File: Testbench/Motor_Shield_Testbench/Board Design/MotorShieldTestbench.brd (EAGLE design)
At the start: 63.5 x 87.6 mm, 49 parts, among them IC2 74LS04D, IC3 74AC74D, IC4 74AC74D, U1 ATMEGA2560AU, U10 +12v, U2 FT232RL, U3 ATTINY85-20SU, U4 ATTINY85-20SU, U6 SN74LVC2G157DCTR, U7 SN74LVC2G157DCTR, U8 SN74LVC2G157DCTR, U9 SN74LVC2G157DCTR, X4 2510-, X5 2510-, X6 MINI-USB_4P-32005-101

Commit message: complete board v1
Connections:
- net LDIR: now also U1.83; no longer U1.76
- net RSPEED: now also U1.84; no longer U1.83
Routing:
- net D+: track 214.0 -> 39.0 mm, vias 0 -> 2
- net +5V: track 509.0 -> 500.6 mm
- net LWAVE1: track 62.6 -> 54.4 mm, vias 6 -> 5
- net GND: track 107.9 -> 102.6 mm
- net D-: track 74.1 -> 69.8 mm
- net RDIR: track 20.2 -> 23.7 mm, vias 3 -> 1
- net TXM: track 15.3 -> 17.5 mm, vias 2 -> 0
- net RXM: track 22.7 -> 21.3 mm
- net LSPEED: track 18.0 -> 19.2 mm, vias 2 -> 0

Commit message: Set layers and DRC
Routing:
- net LWAVE1: track 54.4 -> 56.2 mm

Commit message: minor improvements
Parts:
- moved X5 61.1 mm to (45.0, 11.5)
- moved X4 60.9 mm to (54.0, 11.5), turned to 90 degrees
- moved R13 44.3 mm to (49.0, 59.0)
- moved LED3 42.1 mm to (52.2, 57.5), turned to 270 degrees
- moved R8 39.6 mm to (26.0, 40.0)
- moved R7 38.7 mm to (26.0, 42.0)
- moved LED2 37.4 mm to (22.0, 40.0), turned to 180 degrees
- moved C10 35.0 mm to (10.5, 36.5)
- moved R1 34.2 mm to (39.2, 5.75), turned to 270 degrees
- moved R2 33.0 mm to (39.2, 9.50), turned to 270 degrees
- moved LED1 33.0 mm to (22.0, 42.0), turned to 180 degrees
- moved U10 27.6 mm to (11.5, 58.0), turned to 0 degrees
- moved IC4 27.5 mm to (32.5, 6.50), turned to 270 degrees
- moved IC3 26.6 mm to (32.5, 27.5), turned to 270 degrees
- moved U2 26.5 mm to (14.0, 44.5), turned to 180 degrees
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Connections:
- net LE1: now also U1.4
- net LE2: now also U1.5
- net LSELECT: now also IC2.13; no longer IC2.1
- net LWAVE: now also IC2.11; no longer IC2.9
- net N$14: now also IC2.4; no longer IC2.10
- net N$27: now also IC2.10; no longer IC2.8
- net N$3: now also IC2.2; no longer IC2.4
- net N$8: now also IC2.12; no longer IC2.2
- net RDIR: now also U1.85; no longer U1.77
- net RE1: now also U1.45
- net RE2: now also U1.46
- net RSELECT: now also IC2.1; no longer IC2.3
- net RWAVE: now also IC2.3; no longer IC2.11
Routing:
- net +5V: track 500.6 -> 134.5 mm, vias 10 -> 18
- net LWAVE2: track 116.6 -> 19.2 mm
- net RE2: track 31.3 -> 106.8 mm, vias 0 -> 4
- net D-: track 69.8 -> 5.20 mm
- net RE1: track 18.8 -> 82.7 mm, vias 0 -> 2
- net LDIR: track 11.7 -> 74.2 mm
- net RWAVE1: track 68.7 -> 9.14 mm, vias 2 -> 0
- net LE1: track 21.6 -> 76.5 mm, vias 0 -> 4
- net RDIR: track 23.7 -> 77.8 mm, vias 1 -> 0
- net RSPEEDH: track 6.08 -> 60.2 mm
- net LSPEEDH: track 7.15 -> 55.2 mm
- net GND: track 102.6 -> 55.0 mm, vias 30 -> 42
- net LWAVE1: track 56.2 -> 8.98 mm, vias 5 -> 0
- net RWAVE2: track 63.5 -> 20.3 mm, vias 5 -> 0
- net RSPEED: track 47.0 -> 12.1 mm
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- added copper zone on layer 1, net +5V
- added copper zone on layer 1, net GND
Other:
- board size 63.5 x 87.6 mm -> 60 x 67 mm
- board text added: "MotorShieldTestbench Example Routing"

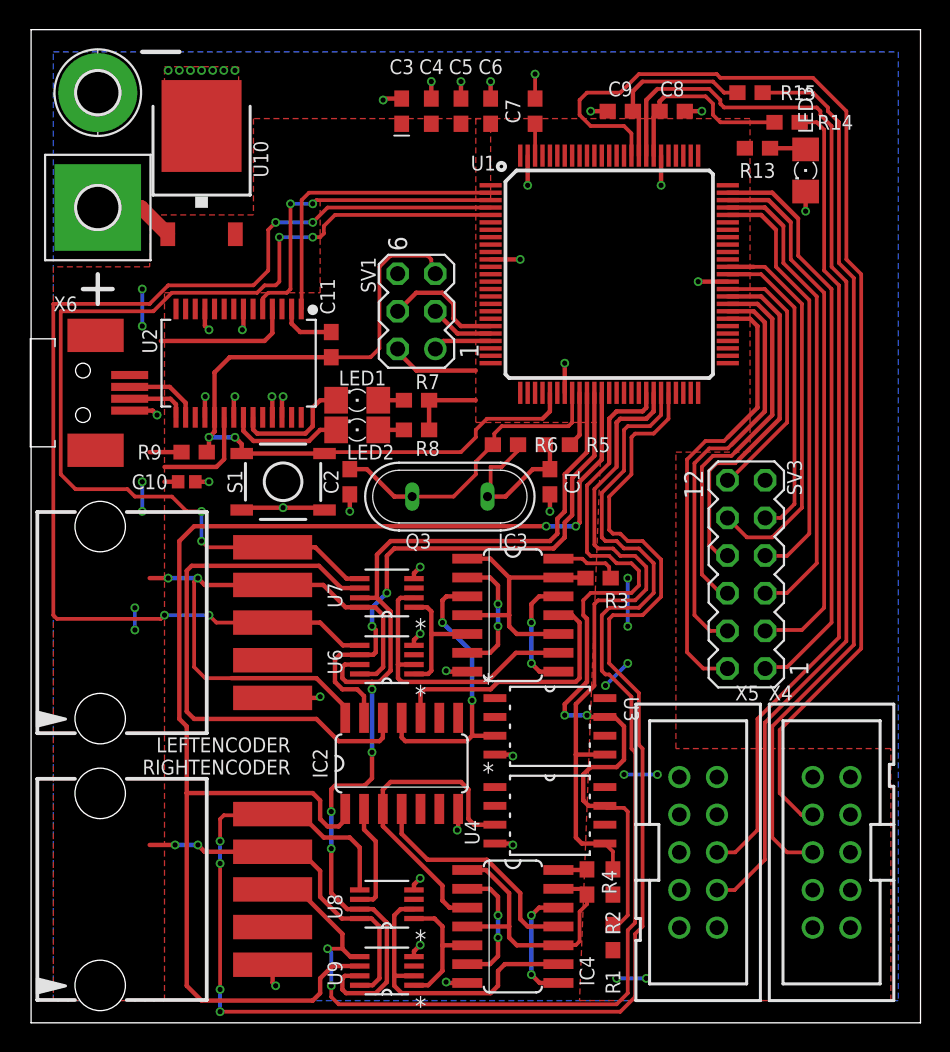
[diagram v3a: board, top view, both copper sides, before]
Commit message: adjusted dimensions
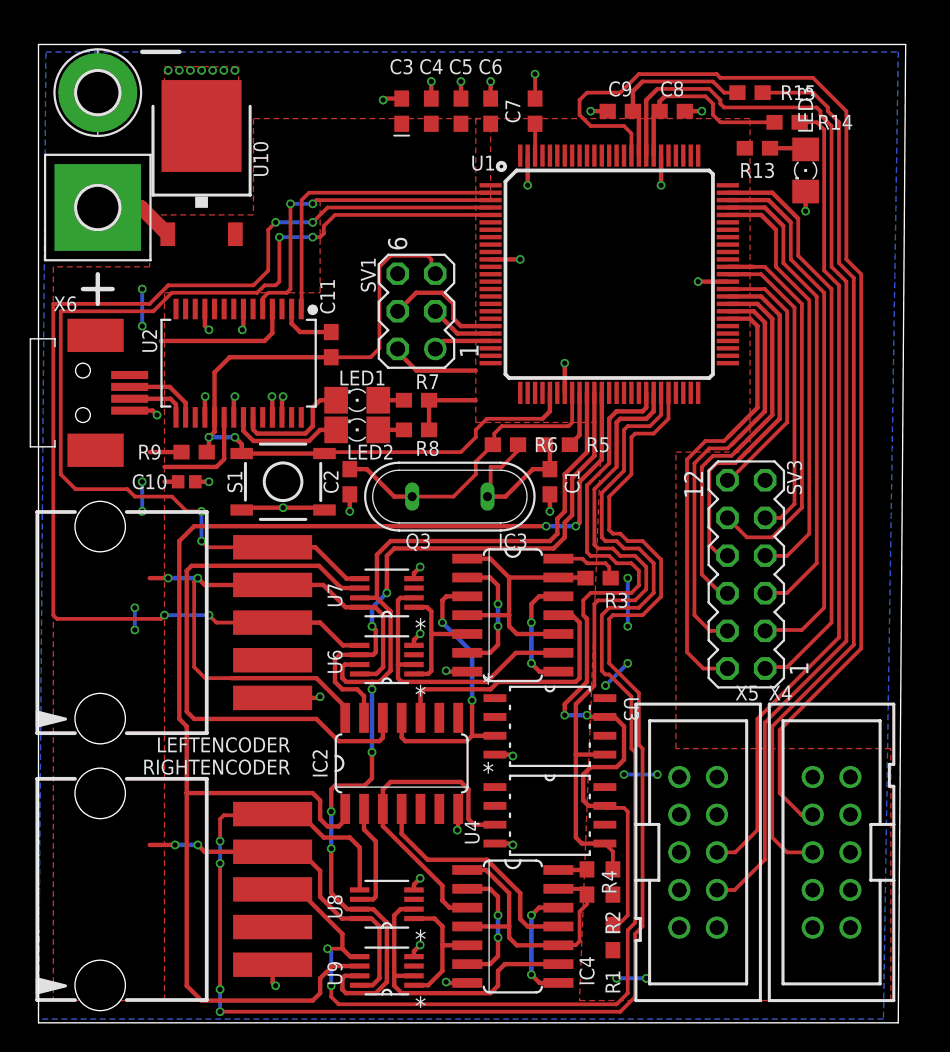
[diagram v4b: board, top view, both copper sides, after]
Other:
- board size 60 x 67 mm -> 58.5 x 66 mm
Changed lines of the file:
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@@
 <board>
 <plain>
-<wire x1="0" y1="0" x2="60" y2="0" width="0" layer="20"/>
-<wire x1="60" y1="0" x2="60" y2="67" width="0" layer="20"/>
-<wire x1="60" y1="67" x2="0" y2="67" width="0" layer="20"/>
-<wire x1="0" y1="67" x2="0" y2="0" width="0" layer="20"/>
+<wire x1="0.5" y1="0" x2="58.5" y2="0" width="0" layer="20"/>
+<wire x1="58.5" y1="0" x2="59" y2="66" width="0" layer="20"/>
+<wire x1="59" y1="66" x2="0.5" y2="66" width="0" layer="20"/>
+<wire x1="0.5" y1="66" x2="0.5" y2="0" width="0" layer="20"/>
 <wire x1="7.5" y1="65.5" x2="10" y2="65.5" width="0.3" layer="21"/>
 <wire x1="4.5" y1="50.5" x2="4.5" y2="49.5" width="0.3" layer="21"/>
@@
 <contactref element="U2" pad="18"/>
 <polygon width="0.5" layer="16" thermals="no">
-<vertex x="58.5" y="1.5"/>
-<vertex x="1.5" y="1.5"/>
-<vertex x="1.5" y="65.5"/>
+<vertex x="57.5" y="0.25"/>
+<vertex x="0.5" y="0.25"/>
+<vertex x="1" y="65.5"/>
 <vertex x="58.5" y="65.5"/>
 </polygon>

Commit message: final schematic v1.0
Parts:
- removed IC2: 74LS04D, 74xx-eu:SO14
- removed LED1, LED2, LED3: (no value), eagle-ltspice:LED_1206
- removed Q3: (no value), special:QS
- removed R2: 10k, SparkFun-Resistors:0603
- removed R5: 27, SparkFun-Resistors:0603
- removed R6: 1M, SparkFun-Resistors:0603
- removed R7: 1k, SparkFun-Resistors:0603
- removed SV1: (no value), con-lstb:MA03-2
- removed SV3: (no value), con-lstb:MA06-2
- removed U10: +12v, SparkFun-IC-Power:TO-252
- removed U6, U7, U8, U9: SN74LVC2G157DCTR, Texas Instruments_By_element14_Batch_1:SOP65P400X130-8N
- added C12, C13: 22pF, SparkFun-Capacitors:0603
- added C14: 1.0uF, SparkFun-Capacitors:0603
- added C15: 10nF, SparkFun-Capacitors:0603
- added C16, C17: 0.1uF, SparkFun-Capacitors:0603
- added D1, D2, D3: (no value), SparkFun-LED:LED-0603
- added IC1: 74LS157D, 74xx-eu:SO16
- added J2: MICRO-SD_CARD_SOCKET, SparkFun-Connectors:MICRO-SD-SOCKET
- added R10, R17: 470, SparkFun-Resistors:0603
- added R11, R16, R18, R21, R22, R23, R24, R25: 10k, SparkFun-Resistors:0603
- added R12: 2.0k, SparkFun-Resistors:0603
- added R19, R20: 47k, SparkFun-Resistors:0603
- added T1: (no value), transistor:SOT23-BEC
- added U$1, U$4: SN74HC153NSR, DigiKey:NS16
- added U$2, U$3: V_REG_LD1117VXX, SparkFun-IC-Power:78XXL
- added X1, X2: C-GRID-05-15-91, con-molex:15-91-05
- added X3: 2520-, con-3m:PAK100/2500-20
- added X7, X8: 2510-, con-3m:PAK100/2500-10
- added Y1: 32.768kHz, SparkFun-Clocks:CRYSTAL-SMD-3.2X1.5MM
- added Y2: 12MHz, SparkFun-Clocks:CRYSTAL-SMD-5X3.2-4PAD
- C1: value 22pF -> 10nF
- C10: device SparkFun-Capacitors:0402 -> SparkFun-Capacitors:0603
- C2: value 22pF -> 1.0uF
- C3: value 10uF -> 22pF; device SparkFun-Capacitors:0603-POLAR -> SparkFun-Capacitors:0603
- C4: value 0.1uF -> 22pF
- R1: value 10k -> 470
- R13: value 1k -> 100k
- R8: value 1k -> 33
- R9: value 10k -> 33
- S1: value MOMENTARY-SWITCH-SPST-SMD-5.2-REDUNDANT -> (none)
- U1: value ATMEGA2560AU -> LPC1768FBD100; device SparkFun-IC-Microcontroller:TQFP100 -> DigiKey:SOT407-1
- U2: value FT232RL -> SN74HC04DR; device SparkFun-IC-Comms:SSOP28DB -> Texas Instruments_By_element14_Batch_1:SOIC127P600X175-14N
- moved R1 162.8 mm to (-115.6, -44.5), turned to 0 degrees
- moved X4 134.8 mm to (-69.8, 64.8), turned to 0 degrees
- moved R4 133.5 mm to (-64.8, 95.2), turned to 0 degrees
- moved C7 126.9 mm to (-90.2, 87.6), turned to 0 degrees
- moved U1 120.3 mm to (-80.0, 33.0)
- moved C6 120.2 mm to (-86.4, 87.6), turned to 0 degrees
- moved R8 119.5 mm to (-80.0, 95.2)
- moved R3 118.7 mm to (-61.0, 95.2)
- moved U3 116.3 mm to (-77.5, 49.5)
- moved C5 114.6 mm to (-82.5, 87.6), turned to 0 degrees
- moved C1 114.4 mm to (-67.3, 87.6), turned to 0 degrees
- moved IC4 111.2 mm to (-52.1, 78.7), turned to 0 degrees
- moved R9 110.5 mm to (-83.8, 95.2), turned to 0 degrees
- moved C4 108.9 mm to (-78.7, 87.6), turned to 0 degrees
- moved C2 105.8 mm to (-71.1, 87.6), turned to 0 degrees
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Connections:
- removed net D+: U2.15, X6.3
- removed net D-: U2.16, X6.2
- removed net DTR: C11.1, U2.2
- removed net LSELECT: IC2.13, U1.36, U6.6
- removed net MISO: SV1.1, U1.22
- removed net MOSI: SV1.3, U1.21
- removed net N$14: IC2.4, IC4.11
- removed net N$36: C7.1, U1.98
- removed net N$37: LED1.A, R7.1
- removed net N$38: LED2.A, R8.1
- removed net N$47: LED3.A, R13.1
- removed net N$63: C1.2, Q3.1, R5.2, R6.1
- removed net OA1: SV3.8, U1.60
- removed net OA2: SV3.6, U1.59
- removed net OA3: SV3.4, U1.58
- removed net OA4: SV3.2, U1.57
- removed net OD1: SV3.7, U1.71
- removed net OD2: SV3.5, U1.72
- removed net OD3: SV3.3, U1.73
- removed net OD4: SV3.1, U1.74
- removed net ORXM: SV3.9, U1.63
- removed net OTXM: SV3.10, U1.64
- removed net RESET: C11.2, R9.1, S1.3, S1.4, SV1.5, U1.30, U2.19
- removed net RSELECT: IC2.1, U1.37, U9.6
- removed net RXLED: LED2.C, U2.22
- removed net RXM: U1.2, U2.1
- removed net SCK: SV1.4, U1.20
- removed net TXLED: LED1.C, U2.23
- removed net TXM: U1.3, U2.5
- new net +3V3: C1.1, C2.1, IC1.16, IC3.14, IC4.14, J2.VCC, R1.1, R11.2, R18.2, R19.2, R20.2, R21.2, R22.2, R23.2, R24.2, R3.2, R4.2, T1.C, U$1.16, U$2.GND, U$3.GND, U$4.16, U1.10, U2.14, U3.8, U4.8, X3.1, X3.2
- new net CONNECT: R12.1, U1.64
- new net DM: R8.1, U1.30
- new net DP: R9.1, U1.29
- new net LDIRIN: IC1.14, U1.7, X8.8
- new net LDIRO: IC1.13, U1.35
- new net LEIN1: U$1.6, U1.70, U3.2, X2.3
- new net LEIN2: U$1.10, U1.69, U3.3, X2.5
- new net LSPEEDIN: IC1.5, R14.1, X8.6
- new net LSPEEDO: U1.37
- new net LWAVE*: IC3.11, U2.2
- new net N$11: J2.RSV2, R20.1
- new net N$13: R9.2, X6.3
- new net N$15: C4.2, U1.18, Y1.P$1
- new net N$16: C3.2, U1.16, Y1.P$2
- new net N$17: C13.2, U1.23, Y2.1
- new net N$18: C12.2, U1.22, Y2.3
- new net N$2: D3.A, R1.2
- new net N$20: D1.A, R8.2, T1.E, X6.2
- new net N$21: R25.2, X3.9
- new net OSMC: IC1.1, U1.39
- new net RDIRIN: IC1.11, U1.6, X7.8
- new net RDIRO: IC1.10, U1.36
- new net REIN1: U$4.6, U1.75, U4.2, X1.3
- new net REIN2: U$4.10, U1.74, U4.3, X1.5
- new net RSPEEDIN: IC1.2, R15.1, X7.6
- new net RSPEEDO: U1.38
- new net RST: C17.1, D2.A, R18.1, S1.3, S1.4, U1.17, U3.1, U4.1, X3.15
- new net RSTOUT: U1.14
- new net RTCK: U1.100
- new net RWAVE*: IC4.11, U2.4
- new net SD_CS: J2.CS, U1.79
- new net SD_DI: J2.DI, U1.76
- new net SD_DO: J2.DO, U1.77
- new net SD_SCK: J2.SCLK, U1.78
- new net SELECT1: U$1.2, U$4.2, U1.63
- new net SELECT2: U$1.14, U$4.14, U1.62
- new net TCK: U1.5, X3.11
- new net TDI: R23.1, U1.2, X3.5
- new net TDO: R21.1, U1.1, X3.13
- new net TMS: R22.1, U1.3, X3.7
- new net TRST: R24.1, U1.4, X3.3
- new net VBUS: R16.1, U1.21
- new net VDD: C10.1, C11.1, C7.1, U1.19, U1.28, U1.54, U1.71, U1.96
- new net VDDR: C5.1, C6.1, U1.42, U1.84
- new net VREFN: C14.2, C15.2, U1.15
- new net VREFP: C14.1, C15.1, U1.12
- net +5V: now also C16.2, R13.1, R16.2, U$3.OUT, X1.4, X2.4, X7.1, X7.2, X7.5, X7.7, X8.1, X8.2, X8.5, X8.7; no longer C10.1, C3.+, C4.1, C5.1, C6.1, IC2.14, IC3.14, IC4.14, R1.2, R13.2, R2.2, R3.2, R4.2, R7.2, R8.2, R9.2, SV1.2, SV3.12, U1.10, U1.100, U1.31, U1.61, U1.80, U10.2, U2.20, U2.4, U3.8, U4.8, U6.8, U7.8, U8.8, U9.8
- net GND: now also C1.2, C11.2, C12.1, C13.1, C16.1, C17.2, C2.2, C3.1, C4.1, IC1.8, J2.GND, J2.GND1, J2.GND3, R10.1, R13.2, R17.1, R25.1, U$1.8, U$2.IN, U$3.IN, U$4.8, U1.31, U1.41, U1.55, U1.72, U1.83, U1.97, X1.1, X2.1, X3.10, X3.12, X3.14, X3.16, X3.18, X3.20, X3.4, X3.6, X3.8, X7.10, X7.9, X8.10, X8.9; no longer C1.1, C2.1, C3.-, C4.2, IC2.7, LED3.C, SV1.6, SV3.11, U1.32, U1.62, U1.81, U1.99, U10.3, U2.11, U2.18, U2.21, U2.25, U2.26, U6.4, U7.4, U8.4, U9.4
- net LDIR: now also IC1.12; no longer U1.83
- net LE1: now also U$1.7; no longer U1.4, U6.5
- net LE2: now also U$1.9; no longer U1.5, U7.5
- net LSPEED: now also IC1.6, U1.9; no longer U1.82
- net LSPEEDH: now also IC1.7; no longer R14.1
- net LWAVE: now also U2.1, U3.6; no longer IC2.11, U3.3
- net LWAVE1: now also U$1.12, U$1.5; no longer U6.1, U7.1
- net LWAVE2: now also U$1.11, U$1.4; no longer U6.2, U7.2
- net N$22: now also R11.1, R12.2, T1.B; no longer R5.1, U1.34
- net N$24: now also D1.C, R10.2; no longer C2.2, Q3.2, R6.2, U1.33
- net N$27: now also D2.C, R17.2; no longer IC2.10, IC3.11
- net N$3: now also D3.C, U1.32; no longer IC2.2, U8.6
- net N$33: now also U$2.OUT; no longer U10.1
- net N$8: now also J2.RSV1, R19.1; no longer IC2.12, U7.6
- net RDIR: now also IC1.9; no longer U1.85
- net RE1: now also U$4.7; no longer U1.45, U9.5
- net RE2: now also U$4.9; no longer U1.46, U8.5
- net RSPEED: now also IC1.3, U1.8; no longer U1.84
- net RSPEEDH: now also IC1.4; no longer R15.1
- net RWAVE: now also U2.3, U4.6; no longer IC2.3, U4.3
- net RWAVE1: now also U$4.12, U$4.5; no longer U8.1, U9.1
- net RWAVE2: now also U$4.11, U$4.4; no longer U8.2, U9.2
- net SCL: now also U1.58; no longer R1.1, U1.43
- net SDA: now also U1.59; no longer R2.1, U1.44
- net STOP: now also IC1.15, U$1.1, U$1.15, U$4.1, U$4.15, U1.61; no longer U1.35, U6.7, U7.7, U8.7, U9.7
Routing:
- net +5V: track 134.5 -> 0.00 mm, vias 18 -> 0
- net RE2: track 106.8 -> 0.00 mm, vias 4 -> 0
- net RSELECT: track 94.0 -> 0.00 mm, vias 2 -> 0
- net RE1: track 82.7 -> 0.00 mm, vias 2 -> 0
- net RDIR: track 77.8 -> 0.00 mm
- net LE1: track 76.5 -> 0.00 mm, vias 4 -> 0
- net LDIR: track 74.2 -> 0.00 mm
- net LE2: track 69.0 -> 0.00 mm, vias 4 -> 0
- net STOP: track 68.7 -> 0.00 mm, vias 4 -> 0
- net RSPEEDH: track 60.2 -> 0.00 mm
- net LSPEEDH: track 55.2 -> 0.00 mm
- net GND: track 55.0 -> 0.00 mm, vias 42 -> 0
- net RESET: track 54.8 -> 0.00 mm, vias 2 -> 0
- net SCL: track 54.2 -> 0.00 mm, vias 2 -> 0
- net SDA: track 44.8 -> 0.00 mm
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- removed copper zone on layer 1, net +5V
- removed copper zone on layer 1, net GND
- removed copper zone on layer 16, net GND
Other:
- board size 58.5 x 66 mm -> 160 x 100 mm
- board text removed: "MotorShieldTestbench Example Routing"

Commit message: Cross Review for schematics
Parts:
- removed C15: 10nF, SparkFun-Capacitors:0603
- added R2, R5: 10k, SparkFun-Resistors:0603
- added U$5: 10uH, inductor-coilcraft:MSS1260
- C14: value 1.0uF -> 0.1uF
- moved C14 225.1 mm to (-129.5, -110.5)
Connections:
- removed net +3V3: C1.1, C2.1, IC1.16, IC3.14, IC4.14, J2.VCC, R1.1, R11.2, R18.2, R19.2, R20.2, R21.2, R22.2, R23.2, R24.2, R3.2, R4.2, T1.C, U$1.16, U$2.GND, U$3.GND, U$4.16, U1.10, U2.14, U3.8, U4.8, X3.1, X3.2
- removed net N$21: R25.2, X3.9
- removed net VREFP: C14.1, C15.1, U1.12
- new net +3V3A: C1.1, C14.2, C2.1, U$5.P$2, U1.10, U1.12
- new net SBL_RXD: R5.2, U1.99, X3.19
- new net SBL_TXD: R2.2, U1.98, X3.17
- net GND: now also C14.1, R2.1, R5.1
- net RTCK: now also R21.1, X3.11
- net TCK: now also R25.2, X3.9; no longer X3.11
- net TDO: no longer R21.1
- net VDD: now also IC1.16, IC3.14, IC4.14, J2.VCC, R1.1, R11.2, R18.2, R19.2, R20.2, R21.2, R22.2, R23.2, R24.2, R3.2, R4.2, T1.C, U$1.16, U$2.GND, U$3.GND, U$4.16, U$5.P$1, U2.14, U3.8, U4.8
- net VREFN: no longer C14.2, C15.2

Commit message: 0.4/10.2017
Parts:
- removed X3: 2520-, con-3m:PAK100/2500-20
- added J1: (no value), SparkFun-Connectors:2X5-SHROUDED
- added R26, R27, R28, R33, R34, R35, R36: 10k, SparkFun-Resistors:0603
- added R29, R30, R31, R32, R6, R7: 1k, SparkFun-Resistors:0603
- added R37, R38: 4.7k, SparkFun-Resistors:0603
- added R40: 200, SparkFun-Resistors:0603
- added SW1: (no value), special:EDG-01
- added U5, U6, U7, U8: DUAL-OPTOISOLATOR_SOIC8, SparkFun-DiscreteSemi:SO08
- R2, R5: value 10k -> 1k
- moved C14 220.2 mm to (-74.9, 102.9)
- moved R5 197.6 mm to (-101.6, 102.9)
- moved R2 195.8 mm to (-90.2, 102.9)
- moved IC1 193.1 mm to (-39.4, 94.0)
- moved X8 189.5 mm to (29.2, 54.6)
- moved R24 189.3 mm to (72.4, 51.2), turned to 90 degrees
- moved U$5 188.1 mm to (-45.7, 69.8)
- moved D3 172.0 mm to (-57.1, 113.0)
- moved U1 164.8 mm to (83.8, 50.8)
- moved R25 150.3 mm to (-83.8, 109.2)
- moved R1 150.2 mm to (-86.4, 102.9)
- moved X7 144.2 mm to (-76.2, 81.3)
- moved R23 143.5 mm to (-76.2, 109.2)
- moved R22 140.3 mm to (-72.4, 109.2)
- moved R21 137.2 mm to (-68.6, 109.2)
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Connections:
- removed net RSTOUT: U1.14
- removed net VDDR: C5.1, C6.1, U1.42, U1.84
- removed net VREFN: U1.15
- new net +3V3: C10.1, C11.1, C5.1, C6.1, C7.1, J1.1, J2.VCC, R1.1, R19.2, R20.2, R21.2, R22.2, R23.2, R37.2, R38.2, U$1.16, U$4.16, U$5.P$1, U1.19, U1.28, U1.42, U1.54, U1.71, U1.84, U1.96, U3.8, U4.8, U5.6, U5.8, U6.6, U6.8
- new net L+12V: U7.6, U7.8, X5.1, X5.2, X5.5, X5.7, X8.1, X8.2, X8.5, X8.7
- new net LDIR1: R33.2, U7.5, X5.8
- new net LDIRIN1: X8.8
- new net LDIRIN3: R28.2, U1.7, U5.5
- new net LGND: U6.2, U6.4, X5.10, X5.9, X8.10, X8.9
- new net LSPEEDH1: R34.2, U7.7, X5.6
- new net LSPEEDIN3: R14.1, R27.2, U1.9, U5.7
- new net N$12: R7.2, U6.3
- new net N$14: R5.2, U5.3
- new net N$19: R2.2, U5.1
- new net N$21: R6.2, U6.1
- new net N$23: R29.2, U7.1
- new net N$25: R30.2, U7.3
- new net N$36: R31.2, U8.1
- new net N$37: R32.2, U8.3
- new net N$7: IC1.1, R40.2, SW1.1
- new net R+12V: U8.6, U8.8, X4.1, X4.2, X4.5, X4.7, X7.1, X7.2, X7.5, X7.7
- new net RDIR1: R35.2, U8.5, X4.8
- new net RDIRIN1: X7.8
- new net RDIRIN3: R26.2, U1.6, U6.5
- new net RGND: U5.2, U5.4, X4.10, X4.9, X7.10, X7.9
- new net RSPEEDH1: R36.2, U8.7, X4.6
- new net RSPEEDIN3: R15.1, R24.2, U1.8, U6.7
- net +5V: no longer X4.1, X4.2, X4.5, X4.7, X5.1, X5.2, X5.5, X5.7, X7.1, X7.2, X7.5, X7.7, X8.1, X8.2, X8.5, X8.7
- net GND: now also J1.3, J1.5, J1.9, R24.1, R26.1, R27.1, R28.1, R33.1, R34.1, R35.1, R36.1, SW1.2, U1.15, U7.2, U7.4, U8.2, U8.4; no longer R2.1, R5.1, X3.10, X3.12, X3.14, X3.16, X3.18, X3.20, X3.4, X3.6, X3.8, X4.10, X4.9, X5.10, X5.9, X7.10, X7.9, X8.10, X8.9
- net LDIR: now also R30.1; no longer X5.8
- net LDIRIN: now also R5.1; no longer U1.7, X8.8
- net LSPEED: now also C9.1, IC1.5, R15.2; no longer IC1.6, U1.9
- net LSPEEDH: now also R29.1; no longer X5.6
- net LSPEEDIN: now also R7.1; no longer IC1.5, R14.1
- net LSPEEDO: now also IC1.6
- net OSMC: now also R40.1; no longer IC1.1
- net RDIR: now also R32.1; no longer X4.8
- net RDIRIN: now also R2.1; no longer U1.6, X7.8
- net RSPEED: now also IC1.2; no longer C9.1, IC1.3, R15.2, U1.8
- net RSPEEDH: now also R31.1; no longer X4.6
- net RSPEEDIN: now also R6.1; no longer IC1.2, R15.1
- net RSPEEDO: now also IC1.3
- net RST: now also J1.10; no longer X3.15
- net RTCK: now also J1.7; no longer X3.11
- net SBL_RXD: no longer R5.2, X3.19
- net SBL_TXD: no longer R2.2, X3.17
- net SCL: now also R38.1
- net SDA: now also R37.1
- net TCK: now also J1.4; no longer X3.9
- net TDI: now also J1.8; no longer X3.5
- net TDO: now also J1.6; no longer X3.13
- net TMS: now also J1.2; no longer X3.7
- net TRST: no longer R24.1, X3.3
- net VDD: no longer C10.1, C11.1, C7.1, J2.VCC, R1.1, R19.2, R20.2, R21.2, R22.2, R23.2, R24.2, U$1.16, U$4.16, U$5.P$1, U1.19, U1.28, U1.54, U1.71, U1.96, U3.8, U4.8
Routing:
- net RDIRIN3: track 0.00 -> 8.25 mm
- net LDIRIN3: track 0.00 -> 6.29 mm
- net RSPEEDIN3: track 0.00 -> 4.34 mm
- net GND: track 0.00 -> 2.96 mm
- net LSPEEDIN3: track 0.00 -> 2.68 mm
